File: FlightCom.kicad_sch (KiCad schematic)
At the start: 50 parts, among them J1 Molex Microfit, J2 Conn_02x03_Counter_Clockwise, U1 TPS62153, U2 W25Q256JVEIQTR, U3 LP5912Q3.3DRVRQ1, U4 USBLC6-2SC6, U5 STM32U575VGTx, X1 1XXD32000MBA

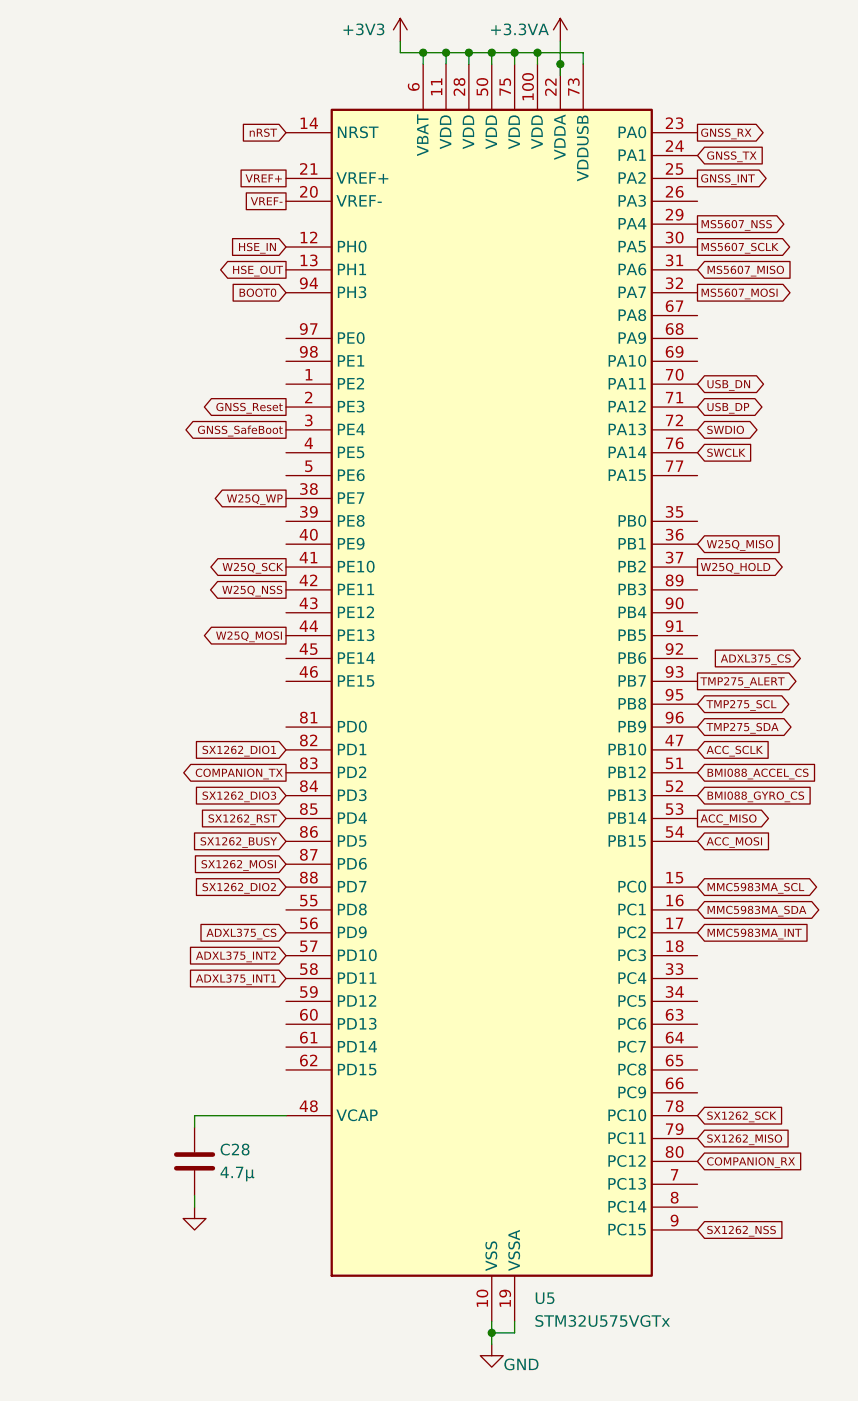
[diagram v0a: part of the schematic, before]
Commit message: reassign pin
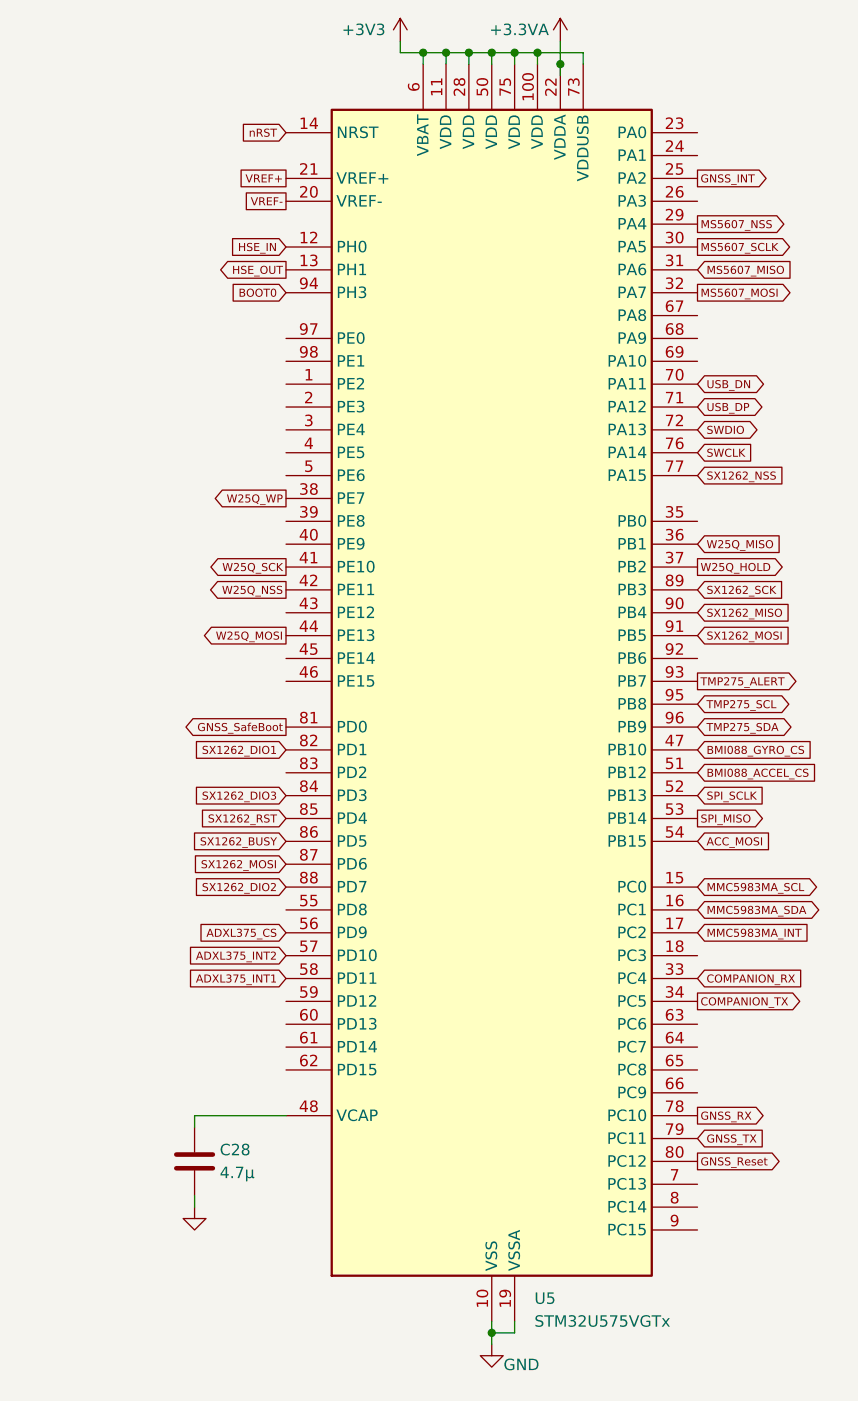
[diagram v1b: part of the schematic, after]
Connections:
- net ACC_SCLK is gone; now on net BMI088_GYRO_CS: U5.47 (PB10)
- net BMI088_GYRO_CS: no longer U5.52 (PB13)
- net COMPANION_RX: now also U5.33 (PC4); no longer U5.80 (PC12)
- net COMPANION_TX: now also U5.34 (PC5); no longer U5.83 (PD2)
- net GNSS_RX: now also U5.78 (PC10); no longer U5.23 (PA0)
- net GNSS_Reset: now also U5.80 (PC12); no longer U5.2 (PE3)
- net GNSS_SafeBoot: now also U5.81 (PD0); no longer U5.3 (PE4)
- net GNSS_TX: now also U5.79 (PC11); no longer U5.24 (PA1)
- net SX1262_MISO: now also U5.90 (PB4); no longer U5.79 (PC11)
- net SX1262_MOSI: now also U5.91 (PB5)
- net SX1262_NSS: now also U5.77 (PA15); no longer U5.9 (PC15)
- net SX1262_SCK: now also U5.89 (PB3); no longer U5.78 (PC10)
- net ACC_MISO renamed SPI_MISO
- new net SPI_SCLK: U5.52 (PB13)

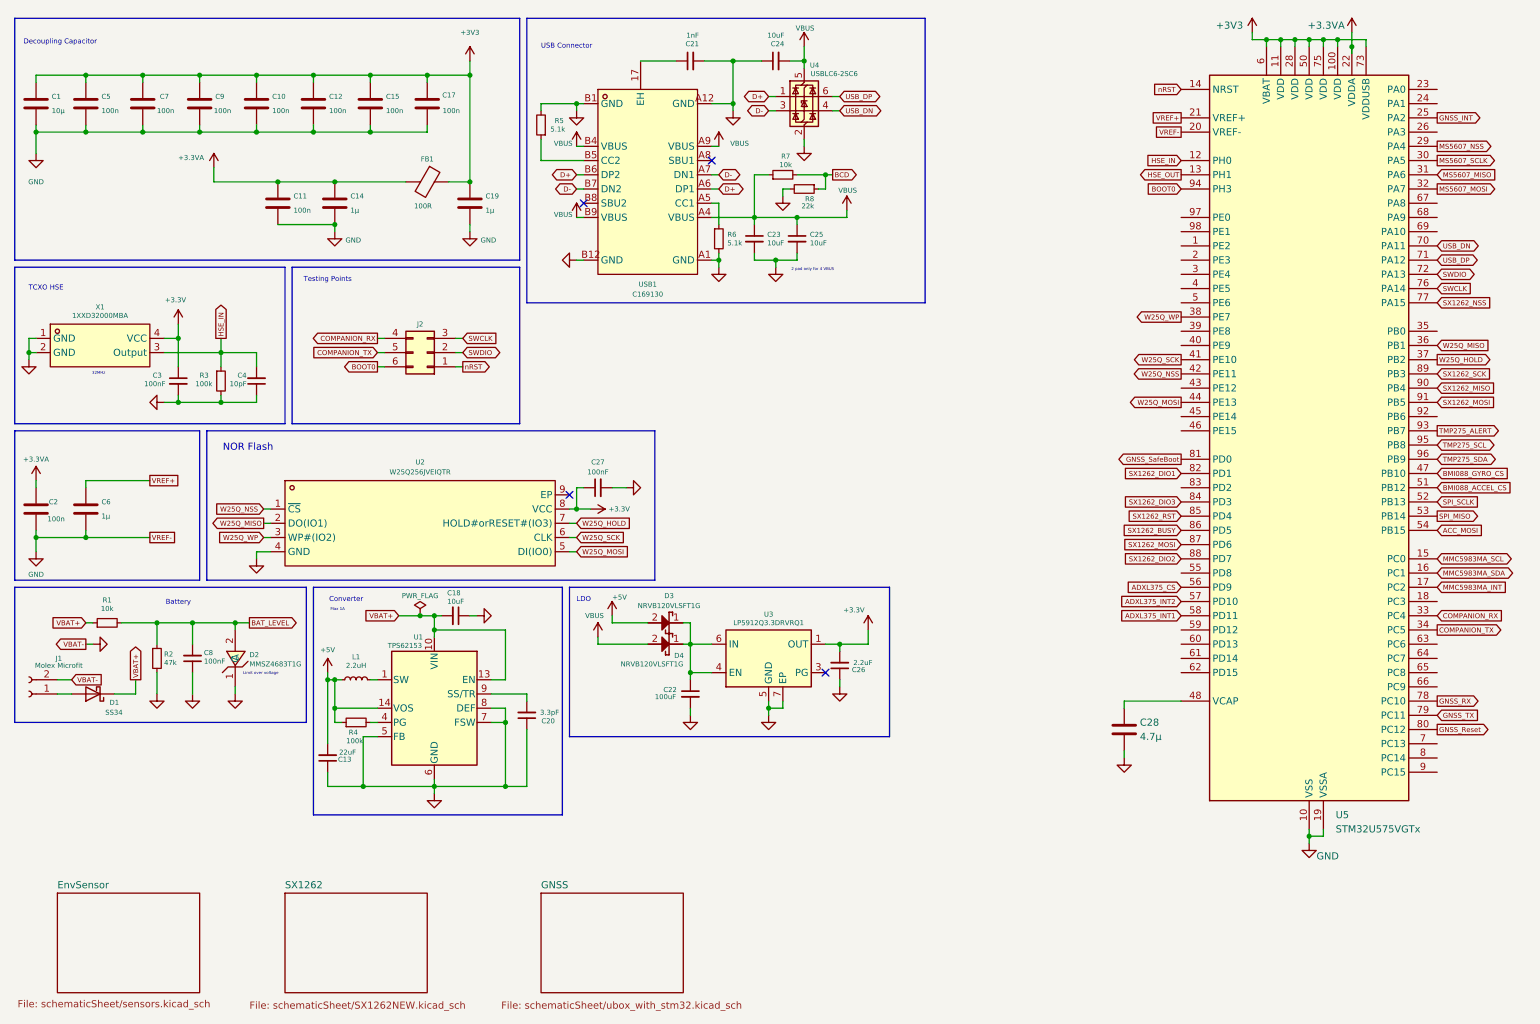
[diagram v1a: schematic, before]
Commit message: reArrange pins
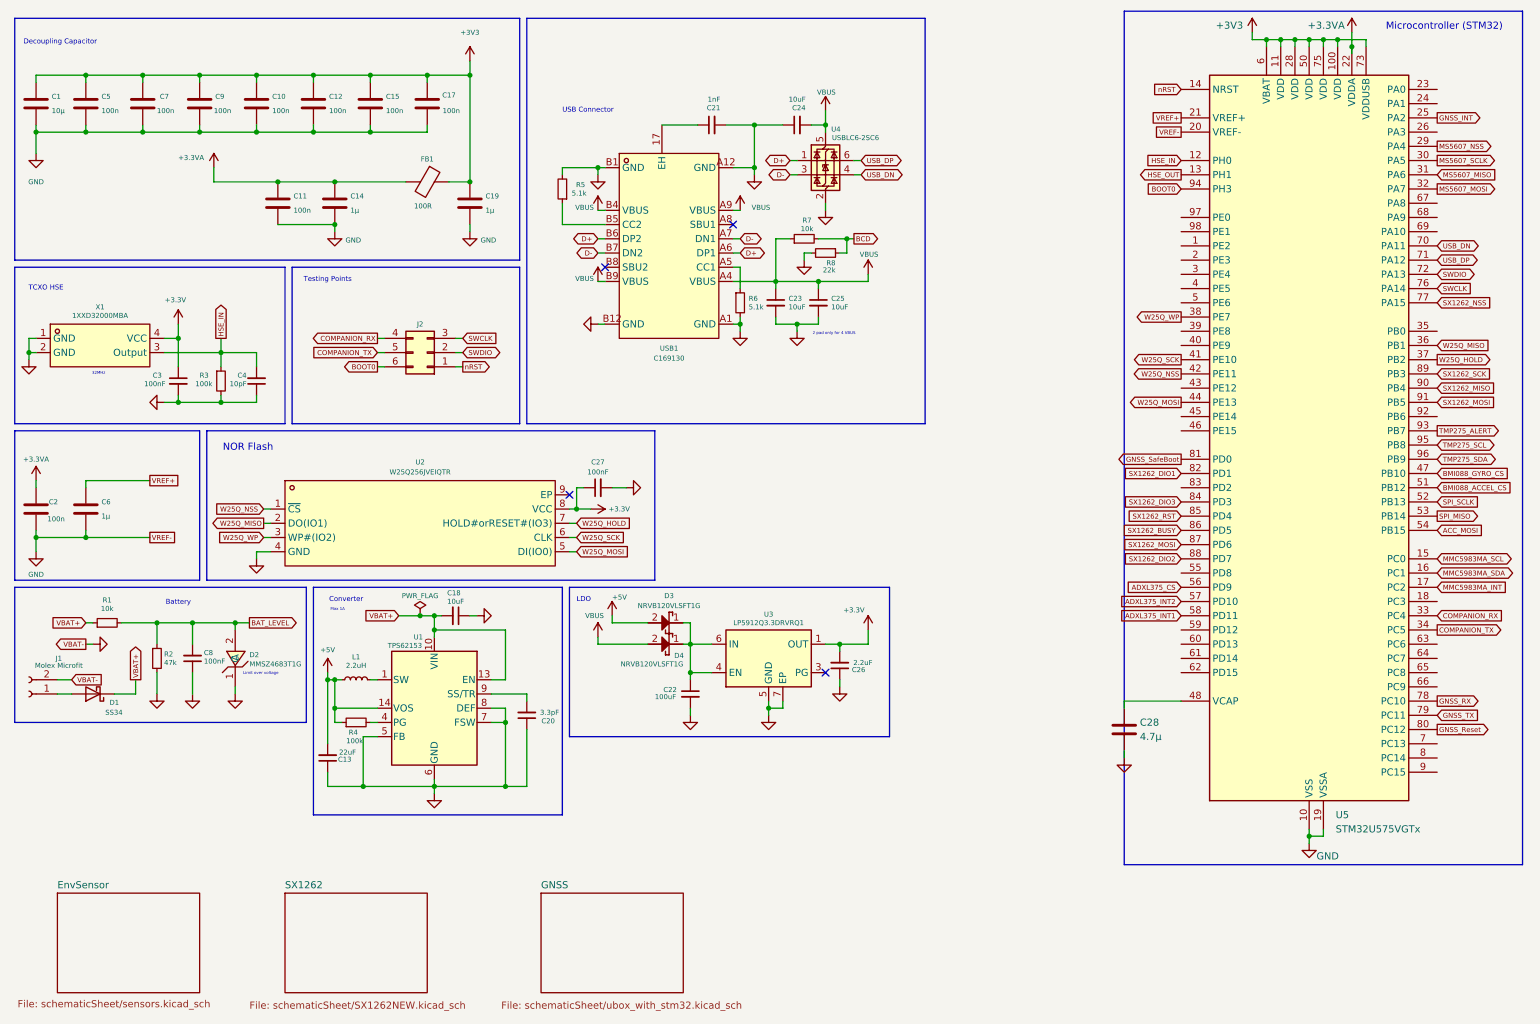
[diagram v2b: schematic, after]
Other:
- note added: "Microcontroller (STM32)"
- moved on the sheet: C21, C23, C24, C25, R5, R6, R7, R8, U4, USB1

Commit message: add power LED
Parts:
- added D9: LED, LED_SMD:LED_0805_2012Metric, symbol Device:LED
- added R22: 1k, Resistor_SMD:R_0805_2012Metric, symbol Device:R
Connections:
- net +3.3V: now also R22.1
- net GND: now also D9.1 (K)
- new net: D9.2 (A), R22.2
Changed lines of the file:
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@@
 	)
 	(junction
+		(at 149.86 139.7)
+		(diameter 0)
+		(color 0 0 0 0)
+	)
+	(junction
 		(at 72.39 132.08)
 		(diameter 0)
@@
 	)
 	(junction
+		(at 162.56 143.51)
+		(diameter 0)
+		(color 0 0 0 0)
+	)
+	(junction
 		(at 243.84 17.78)
 		(diameter 0)
@@
 	)
 	(junction
+		(at 167.64 125.73)
+		(diameter 0)
+		(color 0 0 0 0)
+	)
+	(junction
 		(at 44.45 82.55)
 		(diameter 0)
@@
 	)
 	(junction
-		(at 149.86 137.16)
-		(diameter 0)
-		(color 0 0 0 0)
-	)
-	(junction
 		(at 102.87 151.13)
 		(diameter 0)
@@
 	(wire
 		(pts
+			(xy 162.56 144.78) (xy 162.56 143.51)
+		)
+		(stroke
+			(width 0)
+			(type default)
+		)
+	)
+	(wire
+		(pts
+			(xy 162.56 132.08) (xy 162.56 143.51)
+		)
+		(stroke
+			(width 0)
+			(type default)
+		)
+	)
+	(wire
+		(pts
 			(xy 59.69 101.6) (xy 60.96 101.6)
 		)
@@
 	(wire
 		(pts
-			(xy 149.86 137.16) (xy 149.86 135.89)
+			(xy 149.86 139.7) (xy 149.86 140.97)
 		)
 		(stroke
@@
 	(wire
 		(pts
-			(xy 162.56 132.08) (xy 162.56 133.35)
-		)
-		(stroke
-			(width 0)
-			(type default)
-		)
-	)
-	(wire
-		(pts
 			(xy 119.38 48.26) (xy 120.65 48.26)
 		)
@@
 	(wire
 		(pts
+			(xy 171.45 125.73) (xy 167.64 125.73)
+		)
+		(stroke
+			(width 0)
+			(type default)
+		)
+	)
+	(wire
+		(pts
 			(xy 41.91 71.12) (xy 44.45 71.12)
 		)
@@
 	(wire
 		(pts
+			(xy 149.86 139.7) (xy 149.86 135.89)
+		)
+		(stroke
+			(width 0)
+			(type default)
+		)
+	)
+	(wire
+		(pts
 			(xy 113.03 46.99) (xy 113.03 50.8)
 		)
@@
 	(wire
 		(pts
+			(xy 162.56 143.51) (xy 171.45 143.51)
+		)
+		(stroke
+			(width 0)
+			(type default)
+		)
+	)
+	(wire
+		(pts
 			(xy 135.89 125.73) (xy 139.7 125.73)
 		)
@@
 	(wire
 		(pts
+			(xy 171.45 135.89) (xy 171.45 134.62)
+		)
+		(stroke
+			(width 0)
+			(type default)
+		)
+	)
+	(wire
+		(pts
 			(xy 147.32 40.64) (xy 147.32 41.91)
 		)
@@
 	(wire
 		(pts
-			(xy 149.86 137.16) (xy 149.86 138.43)
-		)
-		(stroke
-			(width 0)
-			(type default)
-		)
-	)
-	(wire
-		(pts
 			(xy 52.07 82.55) (xy 58.42 82.55)
 		)
@@
 	(wire
 		(pts
-			(xy 114.3 104.14) (xy 115.57 104.14)
+			(xy 135.89 137.16) (xy 135.89 140.97)
 		)
 		(stroke
@@
 	(wire
 		(pts
-			(xy 135.89 137.16) (xy 135.89 138.43)
+			(xy 114.3 104.14) (xy 115.57 104.14)
 		)
 		(stroke
@@
 	(wire
 		(pts
+			(xy 171.45 125.73) (xy 171.45 127)
+		)
+		(stroke
+			(width 0)
+			(type default)
+		)
+	)
+	(wire
+		(pts
 			(xy 102.87 123.19) (xy 102.87 132.08)
 		)
@@
 	(wire
 		(pts
-			(xy 152.4 137.16) (xy 149.86 137.16)
+			(xy 152.4 139.7) (xy 149.86 139.7)
 		)
 		(stroke
@@
 	(wire
 		(pts
-			(xy 152.4 137.16) (xy 152.4 135.89)
+			(xy 152.4 139.7) (xy 152.4 135.89)
 		)
 		(stroke
@@
 	(rectangle
 		(start 114.3 115.57)
-		(end 171.45 142.24)
+		(end 179.07 156.21)
 		(stroke
 			(width 0)
@@
 	(symbol
 		(lib_id "power:GND")
-		(at 162.56 133.35 0)
+		(at 162.56 144.78 0)
 		(unit 1)
 		(exclude_from_sim no)
@@
 		(fields_autoplaced yes)
 		(property "Reference" "#PWR036"
-			(at 162.56 139.7 0)
+			(at 162.56 151.13 0)
 			(effects
 				(font
@@
 		)
 		(property "Value" "GND"
-			(at 162.56 138.43 0)
+			(at 162.56 149.86 0)
 			(effects
 				(font
@@
 		)
 		(property "Footprint" ""
-			(at 162.56 133.35 0)
+			(at 162.56 144.78 0)
 			(effects
 				(font
@@
 		)
 		(property "Datasheet" ""
-			(at 162.56 133.35 0)
+			(at 162.56 144.78 0)
 			(effects
 				(font
@@
 		)
 		(property "Description" "Power symbol creates a global label with name \"GND\" , ground"
-			(at 162.56 133.35 0)
+			(at 162.56 144.78 0)
 			(effects
 				(font
@@
 	)
 	(symbol
+		(lib_id "Device:LED")
+		(at 171.45 139.7 90)
+		(unit 1)
+		(exclude_from_sim no)
+		(in_bom yes)
+		(on_board yes)
+		(dnp no)
+		(fields_autoplaced yes)
+		(property "Reference" "D9"
+			(at 175.26 140.0174 90)
+			(effects
+				(font
+					(size 0.889 0.889)
+				)
+				(justify right)
+			)
+		)
+		(property "Value" "LED"
+			(at 175.26 142.5574 90)
+			(effects
+				(font
+					(size 0.889 0.889)
+				)
+				(justify right)
+			)
+		)
+		(property "Footprint" "LED_SMD:LED_0805_2012Metric"
+			(at 171.45 139.7 0)
+			(effects
+				(font
+					(size 1.27 1.27)
+				)
+				(hide yes)
+			)
+		)
+		(property "Datasheet" "~"
+			(at 171.45 139.7 0)
+			(effects
+				(font
+					(size 1.27 1.27)
+				)
+				(hide yes)
+			)
+		)
+		(property "Description" "Light emitting diode"
+			(at 171.45 139.7 0)
+			(effects
+				(font
+					(size 1.27 1.27)
+				)
+				(hide yes)
+			)
+		)
+		(pin "2"
+		)
+		(pin "1"
+		)
+		(instances
+			(project "FlightCom"
+				(path "/f49728bb-5f62-4190-bb7d-54bb4c159a74"
+					(reference "D9")
+					(unit 1)
+				)
+			)
+		)
+	)
+	(symbol
 		(lib_id "power:+3V3")
 		(at 50.8 40.64 0)
@@
 	(symbol
 		(lib_id "power:GND")
-		(at 149.86 138.43 0)
+		(at 149.86 140.97 0)
 		(unit 1)
 		(exclude_from_sim no)
@@
 		(fields_autoplaced yes)
 		(property "Reference" "#PWR031"
-			(at 149.86 144.78 0)
+			(at 149.86 147.32 0)
 			(effects
 				(font
@@
 		)
 		(property "Value" "GND"
-			(at 149.86 143.51 0)
+			(at 149.86 146.05 0)
 			(effects
 				(font
@@
 		)
 		(property "Footprint" ""
-			(at 149.86 138.43 0)
+			(at 149.86 140.97 0)
 			(effects
 				(font
@@
 		)
 		(property "Datasheet" ""
-			(at 149.86 138.43 0)
+			(at 149.86 140.97 0)
 			(effects
 				(font
@@
 		)
 		(property "Description" "Power symbol creates a global label with name \"GND\" , ground"
-			(at 149.86 138.43 0)
+			(at 149.86 140.97 0)
 			(effects
 				(font
@@
 	(symbol
 		(lib_id "power:GND")
-		(at 135.89 138.43 0)
+		(at 135.89 140.97 0)
 		(unit 1)
 		(exclude_from_sim no)
@@
 		(fields_autoplaced yes)
 		(property "Reference" "#PWR027"
-			(at 135.89 144.78 0)
+			(at 135.89 147.32 0)
 			(effects
 				(font
@@
 		)
 		(property "Value" "GND"
-			(at 135.89 143.51 0)
+			(at 135.89 146.05 0)
 			(effects
 				(font
@@
 		)
 		(property "Footprint" ""
-			(at 135.89 138.43 0)
+			(at 135.89 140.97 0)
 			(effects
 				(font
@@
 		)
 		(property "Datasheet" ""
-			(at 135.89 138.43 0)
+			(at 135.89 140.97 0)
 			(effects
 				(font
@@
 		)
 		(property "Description" "Power symbol creates a global label with name \"GND\" , ground"
-			(at 135.89 138.43 0)
+			(at 135.89 140.97 0)
 			(effects
 				(font
@@
 					(unit 1)
 				)
+			)
+		)
+	)
+	(symbol
+		(lib_id "Device:R")
+		(at 171.45 130.81 0)
+		(unit 1)
+		(exclude_from_sim no)
+		(in_bom yes)
+		(on_board yes)
+		(dnp no)
+		(property "Reference" "R22"
+			(at 168.91 131.826 90)
+			(effects
+				(font
+					(size 0.889 0.889)
+				)
+				(justify left)
+			)
+		)
+		(property "Value" "1k"
+			(at 171.45 131.826 90)
+			(effects
+				(font
+					(size 0.889 0.889)
+				)
+				(justify left)
+			)
+		)
+		(property "Footprint" "Resistor_SMD:R_0805_2012Metric"
+			(at 169.672 130.81 90)
+			(effects
+				(font
+					(size 1.27 1.27)
+				)
+				(hide yes)
+			)
+		)
+		(property "Datasheet" "~"
+			(at 171.45 130.81 0)
+			(effects
+				(font
+					(size 1.27 1.27)
+				)
+				(hide yes)
+			)
+		)
+		(property "Description" "Resistor"
+			(at 171.45 130.81 0)
+			(effects
+				(font
+					(size 1.27 1.27)
+				)
+				(hide yes)
+			)
+		)
+		(pin "1"
+		)
+		(pin "2"
+		)
+		(instances
+			(project "FlightCom"
+				(path "/f49728bb-5f62-4190-bb7d-54bb4c159a74"
+					(reference "R22")
+					(unit 1)
+				)

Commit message: update label
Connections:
- net ACC_MOSI renamed SPI_MOSI
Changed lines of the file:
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@@
 	)
 	(rectangle
-		(start 213.36 12.7)
+		(start 209.55 12.7)
 		(end 284.48 165.1)
 		(stroke
@@
 		)
 	)
-	(global_label "ACC_MOSI"
+	(global_label "SPI_MOSI"
 		(shape input)
 		(at 269.24 105.41 0)
@@
 		)
 		(property "Intersheetrefs" "${INTERSHEET_REFS}"
-			(at 277.7641 105.41 0)
-			(effects
-				(font
+			(at 277.3831 105.41 0)
+			(effects
+				(font
